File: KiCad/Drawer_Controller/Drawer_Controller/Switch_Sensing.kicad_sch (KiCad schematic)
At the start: 4 parts

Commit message: More progress
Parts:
- C9: footprint Capacitor_SMD:C_1206_3216Metric_Pad1.33x1.80mm_HandSolder -> Capacitor_SMD:C_0805_2012Metric_Pad1.18x1.45mm_HandSolder
- R13, R14: footprint Resistor_SMD:R_1206_3216Metric_Pad1.30x1.75mm_HandSolder -> Resistor_SMD:R_0805_2012Metric_Pad1.20x1.40mm_HandSolder
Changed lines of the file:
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@@
       (effects (font (size 1.27 1.27)) (justify left))
     )
-    (property "Footprint" "Resistor_SMD:R_1206_3216Metric_Pad1.30x1.75mm_HandSolder" (id 2) (at 130.302 80.645 90)
+    (property "Footprint" "Resistor_SMD:R_0805_2012Metric_Pad1.20x1.40mm_HandSolder" (id 2) (at 130.302 80.645 90)
       (effects (font (size 1.27 1.27)) hide)
     )
@@
       (effects (font (size 1.27 1.27)) (justify left))
     )
-    (property "Footprint" "Capacitor_SMD:C_1206_3216Metric_Pad1.33x1.80mm_HandSolder" (id 2) (at 109.855 87.63 0)
+    (property "Footprint" "Capacitor_SMD:C_0805_2012Metric_Pad1.18x1.45mm_HandSolder" (id 2) (at 109.855 87.63 0)
       (effects (font (size 1.27 1.27)) hide)
     )
@@
     (property "Reference" "R13" (id 0) (at 122.555 80.01 90))
     (property "Value" "10k" (id 1) (at 122.555 82.55 90))
-    (property "Footprint" "Resistor_SMD:R_1206_3216Metric_Pad1.30x1.75mm_HandSolder" (id 2) (at 122.555 85.09 0)
+    (property "Footprint" "Resistor_SMD:R_0805_2012Metric_Pad1.20x1.40mm_HandSolder" (id 2) (at 122.555 85.09 0)
       (effects (font (size 1.27 1.27)) hide)
     )

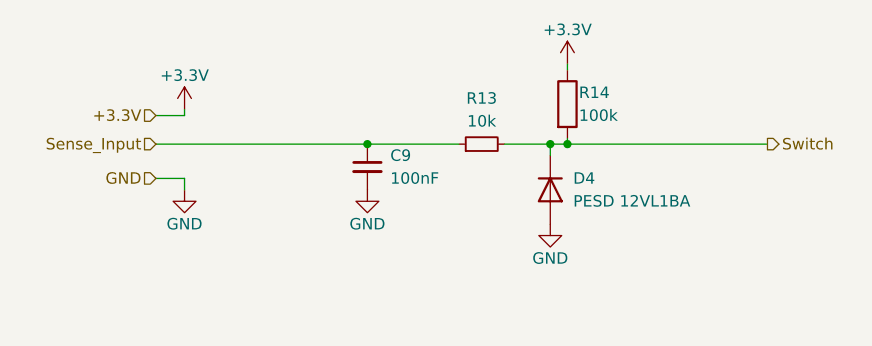
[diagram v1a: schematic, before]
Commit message: Small adjustments after schematic review with Basti
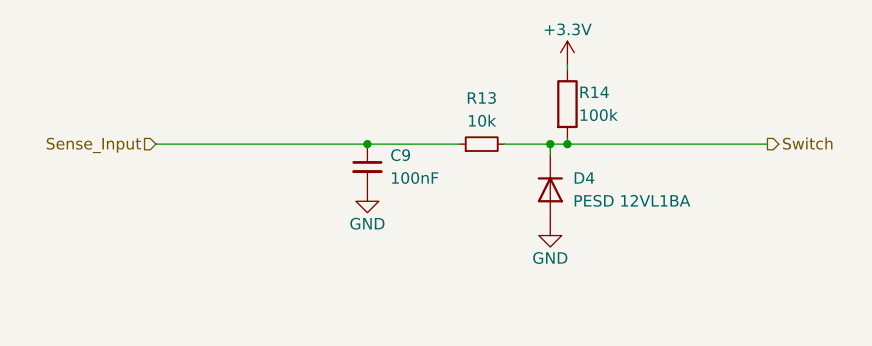
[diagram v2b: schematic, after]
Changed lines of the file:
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@@
-    (stroke (width 0) (type default) (color 0 0 0 0))
-  )
-  (wire (pts (xy 89.535 90.17) (xy 89.535 88.9))
-    (stroke (width 0) (type default) (color 0 0 0 0))
-  )
-  (wire (pts (xy 86.36 81.915) (xy 89.535 81.915))
     (stroke (width 0) (type default) (color 0 0 0 0))
   )
   (wire (pts (xy 132.08 84.455) (xy 132.08 85.09))
-    (stroke (width 0) (type default) (color 0 0 0 0))
-  )
-  (wire (pts (xy 89.535 88.9) (xy 86.36 88.9))
-    (stroke (width 0) (type default) (color 0 0 0 0))
-  )
-  (wire (pts (xy 89.535 81.915) (xy 89.535 81.28))
     (stroke (width 0) (type default) (color 0 0 0 0))
   )
@@
     (stroke (width 0) (type default) (color 0 0 0 0))
   )
-  (hierarchical_label "+3.3V" (shape input) (at 86.36 81.915 180)
-    (effects (font (size 1.27 1.27)) (justify right))
-  )
   (hierarchical_label "Switch" (shape output) (at 154.305 85.09 0)
     (effects (font (size 1.27 1.27)) (justify left))
   )
   (hierarchical_label "Sense_Input" (shape input) (at 86.36 85.09 180)
-    (effects (font (size 1.27 1.27)) (justify right))
-  )
-  (hierarchical_label "GND" (shape input) (at 86.36 88.9 180)
     (effects (font (size 1.27 1.27)) (justify right))
   )
@@
     )
     (property "Datasheet" "" (id 3) (at 109.855 90.17 0)
-      (effects (font (size 1.27 1.27)) hide)
-    )
-    (pin "1")
-  )
-  (symbol (lib_id "power:GND") (at 89.535 90.17 0) (unit 1)
-    (in_bom yes) (on_board yes)
-    (property "Reference" "#PWR0151" (id 0) (at 89.535 96.52 0)
-      (effects (font (size 1.27 1.27)) hide)
-    )
-    (property "Value" "GND" (id 1) (at 89.535 93.98 0))
-    (property "Footprint" "" (id 2) (at 89.535 90.17 0)
-      (effects (font (size 1.27 1.27)) hide)
-    )
-    (property "Datasheet" "" (id 3) (at 89.535 90.17 0)
       (effects (font (size 1.27 1.27)) hide)
     )
@@
       (effects (font (size 1.27 1.27)) hide)
     )
-    (pin "1")
-  )
-  (symbol (lib_id "power:+3.3V") (at 89.535 81.28 0) (unit 1)
-    (in_bom yes) (on_board yes)
-    (property "Reference" "#PWR0152" (id 0) (at 89.535 85.09 0)
-      (effects (font (size 1.27 1.27)) hide)
-    )
-    (property "Value" "+3.3V" (id 1) (at 89.535 77.47 0))
-    (property "Footprint" "" (id 2) (at 89.535 81.28 0)
-      (effects (font (size 1.27 1.27)) hide)
-    )
-    (property "Datasheet" "" (id 3) (at 89.535 81.28 0)
-      (effects (font (size 1.27 1.27)) hide)
-    )

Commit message: Small progress
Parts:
- renumbered C9 to C?, D4 to D?, R14 to R?, R13 to R?
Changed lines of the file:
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@@
     (effects (font (size 1.27 1.27)) (justify right))
   )
-  (symbol (lib_id "power:GND") (at 109.855 90.17 0) (unit 1)
+  (symbol (lib_id "power:GND") (at 109.855 90.17 0)
     (in_bom yes) (on_board yes)
-    (property "Reference" "#PWR0150" (id 0) (at 109.855 96.52 0)
+    (property "Reference" "#PWR?" (id 0) (at 109.855 96.52 0)
       (effects (font (size 1.27 1.27)) hide)
     )
@@
     (pin "1")
   )
-  (symbol (lib_id "power:GND") (at 130.175 93.98 0) (unit 1)
+  (symbol (lib_id "power:GND") (at 130.175 93.98 0)
     (in_bom yes) (on_board yes)
-    (property "Reference" "#PWR0149" (id 0) (at 130.175 100.33 0)
+    (property "Reference" "#PWR?" (id 0) (at 130.175 100.33 0)
       (effects (font (size 1.27 1.27)) hide)
     )
@@
     (pin "1")
   )
-  (symbol (lib_id "Diode:1N4148WS") (at 130.175 90.17 270) (unit 1)
+  (symbol (lib_id "Diode:1N4148WS") (at 130.175 90.17 270)
     (in_bom yes) (on_board yes) (fields_autoplaced)
-    (property "Reference" "D4" (id 0) (at 132.715 88.8999 90)
+    (property "Reference" "D?" (id 0) (at 132.715 88.8999 90)
       (effects (font (size 1.27 1.27)) (justify left))
     )
@@
     (pin "2")
   )
-  (symbol (lib_id "power:+3.3V") (at 132.08 76.2 0) (unit 1)
+  (symbol (lib_id "power:+3.3V") (at 132.08 76.2 0)
     (in_bom yes) (on_board yes)
-    (property "Reference" "#PWR0148" (id 0) (at 132.08 80.01 0)
+    (property "Reference" "#PWR?" (id 0) (at 132.08 80.01 0)
       (effects (font (size 1.27 1.27)) hide)
     )
@@
     (pin "1")
   )
-  (symbol (lib_id "Device:R") (at 132.08 80.645 0) (unit 1)
+  (symbol (lib_id "Device:R") (at 132.08 80.645 0)
     (in_bom yes) (on_board yes)
-    (property "Reference" "R14" (id 0) (at 133.35 79.375 0)
+    (property "Reference" "R?" (id 0) (at 133.35 79.375 0)
       (effects (font (size 1.27 1.27)) (justify left))
     )
@@
     (pin "2")
   )
-  (symbol (lib_id "Device:C_Small") (at 109.855 87.63 0) (unit 1)
+  (symbol (lib_id "Device:C_Small") (at 109.855 87.63 0)
     (in_bom yes) (on_board yes)
-    (property "Reference" "C9" (id 0) (at 112.395 86.36 0)
+    (property "Reference" "C?" (id 0) (at 112.395 86.36 0)
       (effects (font (size 1.27 1.27)) (justify left))
     )
@@
     (pin "2")
   )
-  (symbol (lib_id "Device:R_Small") (at 122.555 85.09 90) (unit 1)
+  (symbol (lib_id "Device:R_Small") (at 122.555 85.09 90)
     (in_bom yes) (on_board yes)
-    (property "Reference" "R13" (id 0) (at 122.555 80.01 90))
+    (property "Reference" "R?" (id 0) (at 122.555 80.01 90))
     (property "Value" "10k" (id 1) (at 122.555 82.55 90))
     (property "Footprint" "Resistor_SMD:R_0805_2012Metric_Pad1.20x1.40mm_HandSolder" (id 2) (at 122.555 85.09 0)

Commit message: Start of routing
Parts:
- gave numbers to parts that had none: 4
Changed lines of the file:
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@@
   (symbol (lib_id "power:GND") (at 109.855 90.17 0)
     (in_bom yes) (on_board yes)
-    (property "Reference" "#PWR?" (id 0) (at 109.855 96.52 0)
+    (property "Reference" "#PWR0155" (id 0) (at 109.855 96.52 0)
       (effects (font (size 1.27 1.27)) hide)
     )
@@
   (symbol (lib_id "power:GND") (at 130.175 93.98 0)
     (in_bom yes) (on_board yes)
-    (property "Reference" "#PWR?" (id 0) (at 130.175 100.33 0)
+    (property "Reference" "#PWR0152" (id 0) (at 130.175 100.33 0)
       (effects (font (size 1.27 1.27)) hide)
     )
@@
   (symbol (lib_id "Diode:1N4148WS") (at 130.175 90.17 270)
     (in_bom yes) (on_board yes) (fields_autoplaced)
-    (property "Reference" "D?" (id 0) (at 132.715 88.8999 90)
+    (property "Reference" "D7" (id 0) (at 132.715 88.8999 90)
       (effects (font (size 1.27 1.27)) (justify left))
     )
@@
   (symbol (lib_id "power:+3.3V") (at 132.08 76.2 0)
     (in_bom yes) (on_board yes)
-    (property "Reference" "#PWR?" (id 0) (at 132.08 80.01 0)
+    (property "Reference" "#PWR0151" (id 0) (at 132.08 80.01 0)
       (effects (font (size 1.27 1.27)) hide)
     )
@@
   (symbol (lib_id "Device:R") (at 132.08 80.645 0)
     (in_bom yes) (on_board yes)
-    (property "Reference" "R?" (id 0) (at 133.35 79.375 0)
+    (property "Reference" "R28" (id 0) (at 133.35 79.375 0)
       (effects (font (size 1.27 1.27)) (justify left))
     )
@@
   (symbol (lib_id "Device:C_Small") (at 109.855 87.63 0)
     (in_bom yes) (on_board yes)
-    (property "Reference" "C?" (id 0) (at 112.395 86.36 0)
+    (property "Reference" "C13" (id 0) (at 112.395 86.36 0)
       (effects (font (size 1.27 1.27)) (justify left))
     )
@@
   (symbol (lib_id "Device:R_Small") (at 122.555 85.09 90)
     (in_bom yes) (on_board yes)
-    (property "Reference" "R?" (id 0) (at 122.555 80.01 90))
+    (property "Reference" "R27" (id 0) (at 122.555 80.01 90))
     (property "Value" "10k" (id 1) (at 122.555 82.55 90))
     (property "Footprint" "Resistor_SMD:R_0805_2012Metric_Pad1.20x1.40mm_HandSolder" (id 2) (at 122.555 85.09 0)

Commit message: wip
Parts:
- renumbered C13 to C9, D7 to D4, R27 to R13, R28 to R14
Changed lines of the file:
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@@
   (symbol (lib_id "power:GND") (at 109.855 90.17 0)
     (in_bom yes) (on_board yes)
-    (property "Reference" "#PWR0155" (id 0) (at 109.855 96.52 0)
+    (property "Reference" "#PWR0150" (id 0) (at 109.855 96.52 0)
       (effects (font (size 1.27 1.27)) hide)
     )
@@
   (symbol (lib_id "power:GND") (at 130.175 93.98 0)
     (in_bom yes) (on_board yes)
-    (property "Reference" "#PWR0152" (id 0) (at 130.175 100.33 0)
+    (property "Reference" "#PWR0149" (id 0) (at 130.175 100.33 0)
       (effects (font (size 1.27 1.27)) hide)
     )
@@
   (symbol (lib_id "Diode:1N4148WS") (at 130.175 90.17 270)
     (in_bom yes) (on_board yes) (fields_autoplaced)
-    (property "Reference" "D7" (id 0) (at 132.715 88.8999 90)
+    (property "Reference" "D4" (id 0) (at 132.715 88.8999 90)
       (effects (font (size 1.27 1.27)) (justify left))
     )
@@
   (symbol (lib_id "power:+3.3V") (at 132.08 76.2 0)
     (in_bom yes) (on_board yes)
-    (property "Reference" "#PWR0151" (id 0) (at 132.08 80.01 0)
+    (property "Reference" "#PWR0148" (id 0) (at 132.08 80.01 0)
       (effects (font (size 1.27 1.27)) hide)
     )
@@
   (symbol (lib_id "Device:R") (at 132.08 80.645 0)
     (in_bom yes) (on_board yes)
-    (property "Reference" "R28" (id 0) (at 133.35 79.375 0)
+    (property "Reference" "R14" (id 0) (at 133.35 79.375 0)
       (effects (font (size 1.27 1.27)) (justify left))
     )
@@
   (symbol (lib_id "Device:C_Small") (at 109.855 87.63 0)
     (in_bom yes) (on_board yes)
-    (property "Reference" "C13" (id 0) (at 112.395 86.36 0)
+    (property "Reference" "C9" (id 0) (at 112.395 86.36 0)
       (effects (font (size 1.27 1.27)) (justify left))
     )
@@
   (symbol (lib_id "Device:R_Small") (at 122.555 85.09 90)
     (in_bom yes) (on_board yes)
-    (property "Reference" "R27" (id 0) (at 122.555 80.01 90))
+    (property "Reference" "R13" (id 0) (at 122.555 80.01 90))
     (property "Value" "10k" (id 1) (at 122.555 82.55 90))
     (property "Footprint" "Resistor_SMD:R_0805_2012Metric_Pad1.20x1.40mm_HandSolder" (id 2) (at 122.555 85.09 0)

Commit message: more progress, routing almost done
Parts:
- renumbered C9 to C12, D4 to D6, R13 to R25, R14 to R26
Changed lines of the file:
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@@
   (symbol (lib_id "power:GND") (at 109.855 90.17 0)
     (in_bom yes) (on_board yes)
-    (property "Reference" "#PWR0150" (id 0) (at 109.855 96.52 0)
+    (property "Reference" "#PWR0147" (id 0) (at 109.855 96.52 0)
       (effects (font (size 1.27 1.27)) hide)
     )
@@
   (symbol (lib_id "power:GND") (at 130.175 93.98 0)
     (in_bom yes) (on_board yes)
-    (property "Reference" "#PWR0149" (id 0) (at 130.175 100.33 0)
+    (property "Reference" "#PWR0146" (id 0) (at 130.175 100.33 0)
       (effects (font (size 1.27 1.27)) hide)
     )
@@
   (symbol (lib_id "Diode:1N4148WS") (at 130.175 90.17 270)
     (in_bom yes) (on_board yes) (fields_autoplaced)
-    (property "Reference" "D4" (id 0) (at 132.715 88.8999 90)
+    (property "Reference" "D6" (id 0) (at 132.715 88.8999 90)
       (effects (font (size 1.27 1.27)) (justify left))
     )
@@
   (symbol (lib_id "power:+3.3V") (at 132.08 76.2 0)
     (in_bom yes) (on_board yes)
-    (property "Reference" "#PWR0148" (id 0) (at 132.08 80.01 0)
+    (property "Reference" "#PWR0145" (id 0) (at 132.08 80.01 0)
       (effects (font (size 1.27 1.27)) hide)
     )
@@
   (symbol (lib_id "Device:R") (at 132.08 80.645 0)
     (in_bom yes) (on_board yes)
-    (property "Reference" "R14" (id 0) (at 133.35 79.375 0)
+    (property "Reference" "R26" (id 0) (at 133.35 79.375 0)
       (effects (font (size 1.27 1.27)) (justify left))
     )
@@
   (symbol (lib_id "Device:C_Small") (at 109.855 87.63 0)
     (in_bom yes) (on_board yes)
-    (property "Reference" "C9" (id 0) (at 112.395 86.36 0)
+    (property "Reference" "C12" (id 0) (at 112.395 86.36 0)
       (effects (font (size 1.27 1.27)) (justify left))
     )
@@
   (symbol (lib_id "Device:R_Small") (at 122.555 85.09 90)
     (in_bom yes) (on_board yes)
-    (property "Reference" "R13" (id 0) (at 122.555 80.01 90))
+    (property "Reference" "R25" (id 0) (at 122.555 80.01 90))
     (property "Value" "10k" (id 1) (at 122.555 82.55 90))
     (property "Footprint" "Resistor_SMD:R_0805_2012Metric_Pad1.20x1.40mm_HandSolder" (id 2) (at 122.555 85.09 0)

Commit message: Exported gerbers and small refinements
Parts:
- removed D6: PESD 12VL1BA, Diode_SMD:D_SOD-323, symbol Diode:1N4148WS
- added U9: SMF05CT1G, SMF05CT1G:SOT65P210X110-6N, symbol SMF05CT1G:SMF05CT1G
- renumbered C12 to C13, R25 to R27, R26 to R28
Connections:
- net GND: now also U9.2
- net Switch: now also U9.1, U9.3, U9.4, U9.5, U9.6
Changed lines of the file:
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@@
 (kicad_sch (version 20211123) (generator eeschema)
   (paper "A4")
-  (junction (at 130.175 85.09) (diameter 0) (color 0 0 0 0)
+  (junction (at 139.7 85.09) (diameter 0) (color 0 0 0 0)
+  )
+  (junction (at 143.51 85.09) (diameter 0) (color 0 0 0 0)
+  )
+  (junction (at 134.62 85.09) (diameter 0) (color 0 0 0 0)
   )
   (junction (at 109.855 85.09) (diameter 0) (color 0 0 0 0)
   )
+  (junction (at 130.81 85.09) (diameter 0) (color 0 0 0 0)
+  )
+  (junction (at 137.16 85.09) (diameter 0) (color 0 0 0 0)
+  )
   (junction (at 132.08 85.09) (diameter 0) (color 0 0 0 0)
   )
-  (wire (pts (xy 132.08 85.09) (xy 154.305 85.09))
+  (wire (pts (xy 143.51 85.09) (xy 154.305 85.09))
     (stroke (width 0) (type default) (color 0 0 0 0))
   )
-  (wire (pts (xy 130.175 85.09) (xy 130.175 86.36))
+  (wire (pts (xy 132.08 85.09) (xy 134.62 85.09))
+    (stroke (width 0) (type default) (color 0 0 0 0))
+  )
+  (wire (pts (xy 134.62 85.09) (xy 137.16 85.09))
+    (stroke (width 0) (type default) (color 0 0 0 0))
+  )
+  (wire (pts (xy 130.81 85.09) (xy 132.08 85.09))
     (stroke (width 0) (type default) (color 0 0 0 0))
   )
@@
     (stroke (width 0) (type default) (color 0 0 0 0))
   )
+  (wire (pts (xy 139.7 100.33) (xy 143.51 100.33))
+    (stroke (width 0) (type default) (color 0 0 0 0))
+  )
+  (wire (pts (xy 130.81 85.09) (xy 130.81 100.33))
+    (stroke (width 0) (type default) (color 0 0 0 0))
+  )
   (wire (pts (xy 86.36 85.09) (xy 109.855 85.09))
     (stroke (width 0) (type default) (color 0 0 0 0))
   )
-  (wire (pts (xy 132.08 85.09) (xy 130.175 85.09))
+  (wire (pts (xy 125.095 85.09) (xy 130.81 85.09))
     (stroke (width 0) (type default) (color 0 0 0 0))
   )
@@
     (stroke (width 0) (type default) (color 0 0 0 0))
   )
-  (wire (pts (xy 125.095 85.09) (xy 130.175 85.09))
+  (wire (pts (xy 137.16 85.09) (xy 139.7 85.09))
+    (stroke (width 0) (type default) (color 0 0 0 0))
+  )
+  (wire (pts (xy 139.7 85.09) (xy 143.51 85.09))
+    (stroke (width 0) (type default) (color 0 0 0 0))
+  )
+  (wire (pts (xy 143.51 100.33) (xy 143.51 85.09))
+    (stroke (width 0) (type default) (color 0 0 0 0))
+  )
+  (wire (pts (xy 130.81 100.33) (xy 134.62 100.33))
     (stroke (width 0) (type default) (color 0 0 0 0))
   )
@@
   (symbol (lib_id "power:GND") (at 109.855 90.17 0)
     (in_bom yes) (on_board yes)
-    (property "Reference" "#PWR0147" (id 0) (at 109.855 96.52 0)
+    (property "Reference" "#PWR0155" (id 0) (at 109.855 96.52 0)
       (effects (font (size 1.27 1.27)) hide)
     )
@@
     (pin "1")
   )
-  (symbol (lib_id "power:GND") (at 130.175 93.98 0)
+  (symbol (lib_id "power:GND") (at 137.16 100.33 0)
     (in_bom yes) (on_board yes)
-    (property "Reference" "#PWR0146" (id 0) (at 130.175 100.33 0)
+    (property "Reference" "#PWR0152" (id 0) (at 137.16 106.68 0)
       (effects (font (size 1.27 1.27)) hide)
     )
-    (property "Value" "GND" (id 1) (at 130.175 97.79 0))
-    (property "Footprint" "" (id 2) (at 130.175 93.98 0)
+    (property "Value" "GND" (id 1) (at 137.16 104.14 0))
+    (property "Footprint" "" (id 2) (at 137.16 100.33 0)
       (effects (font (size 1.27 1.27)) hide)
     )
-    (property "Datasheet" "" (id 3) (at 130.175 93.98 0)
+    (property "Datasheet" "" (id 3) (at 137.16 100.33 0)
       (effects (font (size 1.27 1.27)) hide)
     )
     (pin "1")
   )
-  (symbol (lib_id "Diode:1N4148WS") (at 130.175 90.17 270)
+  (symbol (lib_id "SMF05CT1G:SMF05CT1G") (at 137.16 92.71 90)
     (in_bom yes) (on_board yes) (fields_autoplaced)
-    (property "Reference" "D6" (id 0) (at 132.715 88.8999 90)
-      (effects (font (size 1.27 1.27)) (justify left))
+    (property "Reference" "U9" (id 0) (at 143.51 91.4399 90)
+      (effects (font (size 1.27 1.27)) (justify right))
     )
-    (property "Value" "PESD 12VL1BA" (id 1) (at 132.715 91.4399 90)
-      (effects (font (size 1.27 1.27)) (justify left))
+    (property "Value" "SMF05CT1G" (id 1) (at 143.51 93.9799 90)
+      (effects (font (size 1.27 1.27)) (justify right))
     )
-    (property "Footprint" "Diode_SMD:D_SOD-323" (id 2) (at 125.73 90.17 0)
-      (effects (font (size 1.27 1.27)) hide)
+    (property "Footprint" "SMF05CT1G:SOT65P210X110-6N" (id 2) (at 137.16 92.71 0)
+      (effects (font (size 1.27 1.27)) (justify left bottom) hide)
     )
-    (property "Datasheet" "" (id 3) (at 130.175 90.17 0)
-      (effects (font (size 0 0)) hide)
+    (property "Datasheet" "" (id 3) (at 137.16 92.71 0)
+      (effects (font (size 1.27 1.27)) (justify left bottom) hide)
+    )
+    (property "PRICE" "None" (id 4) (at 137.16 92.71 0)
+      (effects (font (size 1.27 1.27)) (justify left bottom) hide)
+    )
+    (property "MP" "SMF05CT1G" (id 5) (at 137.16 92.71 0)
+      (effects (font (size 1.27 1.27)) (justify left bottom) hide)
+    )
+    (property "PACKAGE" "SOT-363 ON Semiconductor" (id 6) (at 137.16 92.71 0)
+      (effects (font (size 1.27 1.27)) (justify left bottom) hide)
+    )
+    (property "STANDARD" "IPC7351B" (id 7) (at 137.16 92.71 0)
+      (effects (font (size 1.27 1.27)) (justify left bottom) hide)
+    )
+    (property "DESCRIPTION" "SMF05C Series 7.2 V 100 W 5-Line Transient Voltage Suppressor Array - SC-88" (id 8) (at 137.16 92.71 0)
+      (effects (font (size 1.27 1.27)) (justify left bottom) hide)
+    )
+    (property "MANUFACTURER" "ON Semiconductor" (id 9) (at 137.16 92.71 0)
+      (effects (font (size 1.27 1.27)) (justify left bottom) hide)
     )
     (pin "1")
     (pin "2")
+    (pin "3")
+    (pin "4")
+    (pin "5")
+    (pin "6")
   )
   (symbol (lib_id "power:+3.3V") (at 132.08 76.2 0)
     (in_bom yes) (on_board yes)
-    (property "Reference" "#PWR0145" (id 0) (at 132.08 80.01 0)
+    (property "Reference" "#PWR0151" (id 0) (at 132.08 80.01 0)
       (effects (font (size 1.27 1.27)) hide)
     )
@@
   (symbol (lib_id "Device:R") (at 132.08 80.645 0)
     (in_bom yes) (on_board yes)
-    (property "Reference" "R26" (id 0) (at 133.35 79.375 0)
+    (property "Reference" "R28" (id 0) (at 133.35 79.375 0)
       (effects (font (size 1.27 1.27)) (justify left))
     )
@@
   (symbol (lib_id "Device:C_Small") (at 109.855 87.63 0)
     (in_bom yes) (on_board yes)
-    (property "Reference" "C12" (id 0) (at 112.395 86.36 0)
+    (property "Reference" "C13" (id 0) (at 112.395 86.36 0)
       (effects (font (size 1.27 1.27)) (justify left))
     )
@@
   (symbol (lib_id "Device:R_Small") (at 122.555 85.09 90)
     (in_bom yes) (on_board yes)
-    (property "Reference" "R25" (id 0) (at 122.555 80.01 90))
+    (property "Reference" "R27" (id 0) (at 122.555 80.01 90))
     (property "Value" "10k" (id 1) (at 122.555 82.55 90))
     (property "Footprint" "Resistor_SMD:R_0805_2012Metric_Pad1.20x1.40mm_HandSolder" (id 2) (at 122.555 85.09 0)
